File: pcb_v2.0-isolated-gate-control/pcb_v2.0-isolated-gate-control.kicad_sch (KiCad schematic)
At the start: 94 parts, among them J1 ServoLock, J10 Buttons, J11 2x encoder, J12 Screw_Terminal_01x06, J13 Relay VFD2 [NO, COM, NC], J14 GND-P, J15 Power-Servo-12V, J16 Power-LightBarrier-12V, J17 3V3 5V VDD, J18 GNDD, J2 supply, J3 12V-filtered, J4 light-barrier, reserve, J5 GND-P, J6 2x remoteControl, J7 Relay VFD1 [NO, COM, NC], J8 RS485, J9 limit, K1 RT314A24, K2 RT314A24, Q1 2N7000, Q2 2N7000, Q3 IRF5305, Q6 IRF5305, U1 esp32-devkit-v1_30Pin, U4 MAX485E, U5 L78S05CV_TO220, U6 ULN2803A

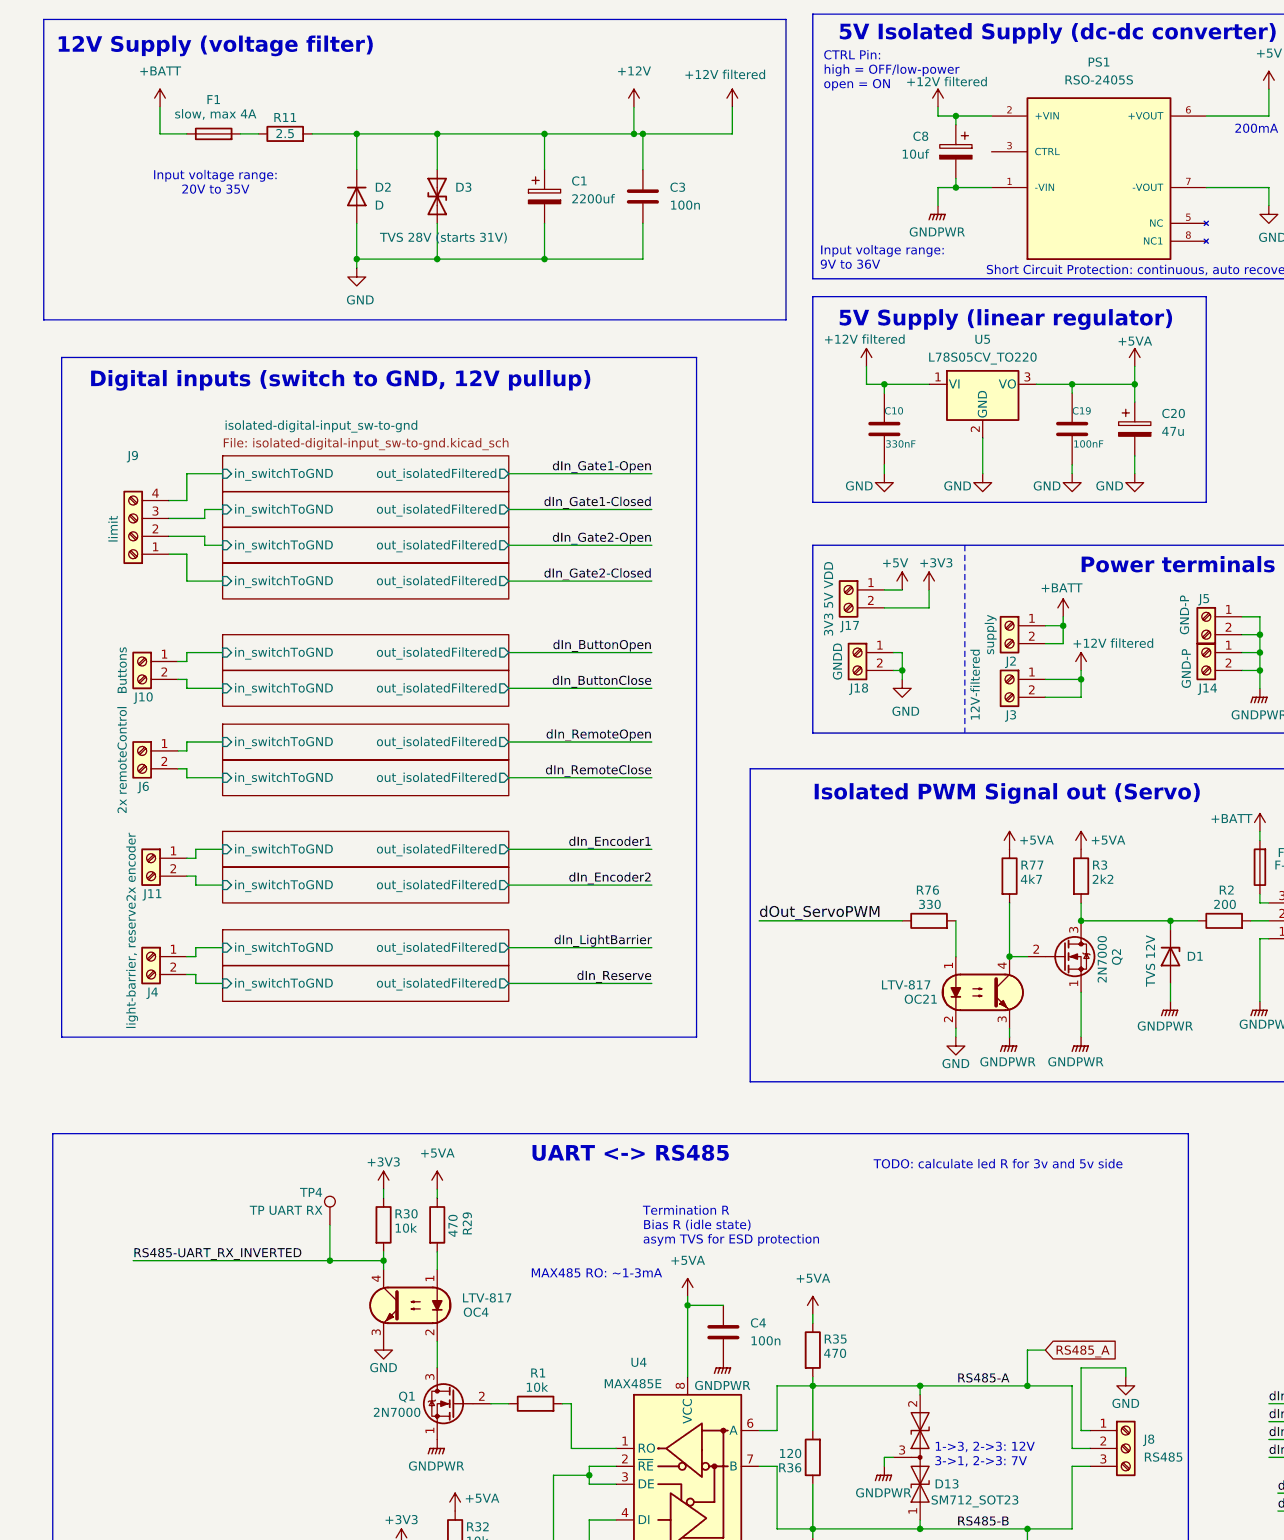
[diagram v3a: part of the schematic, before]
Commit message: pcb: change footprints + arrange groups individually for saving space
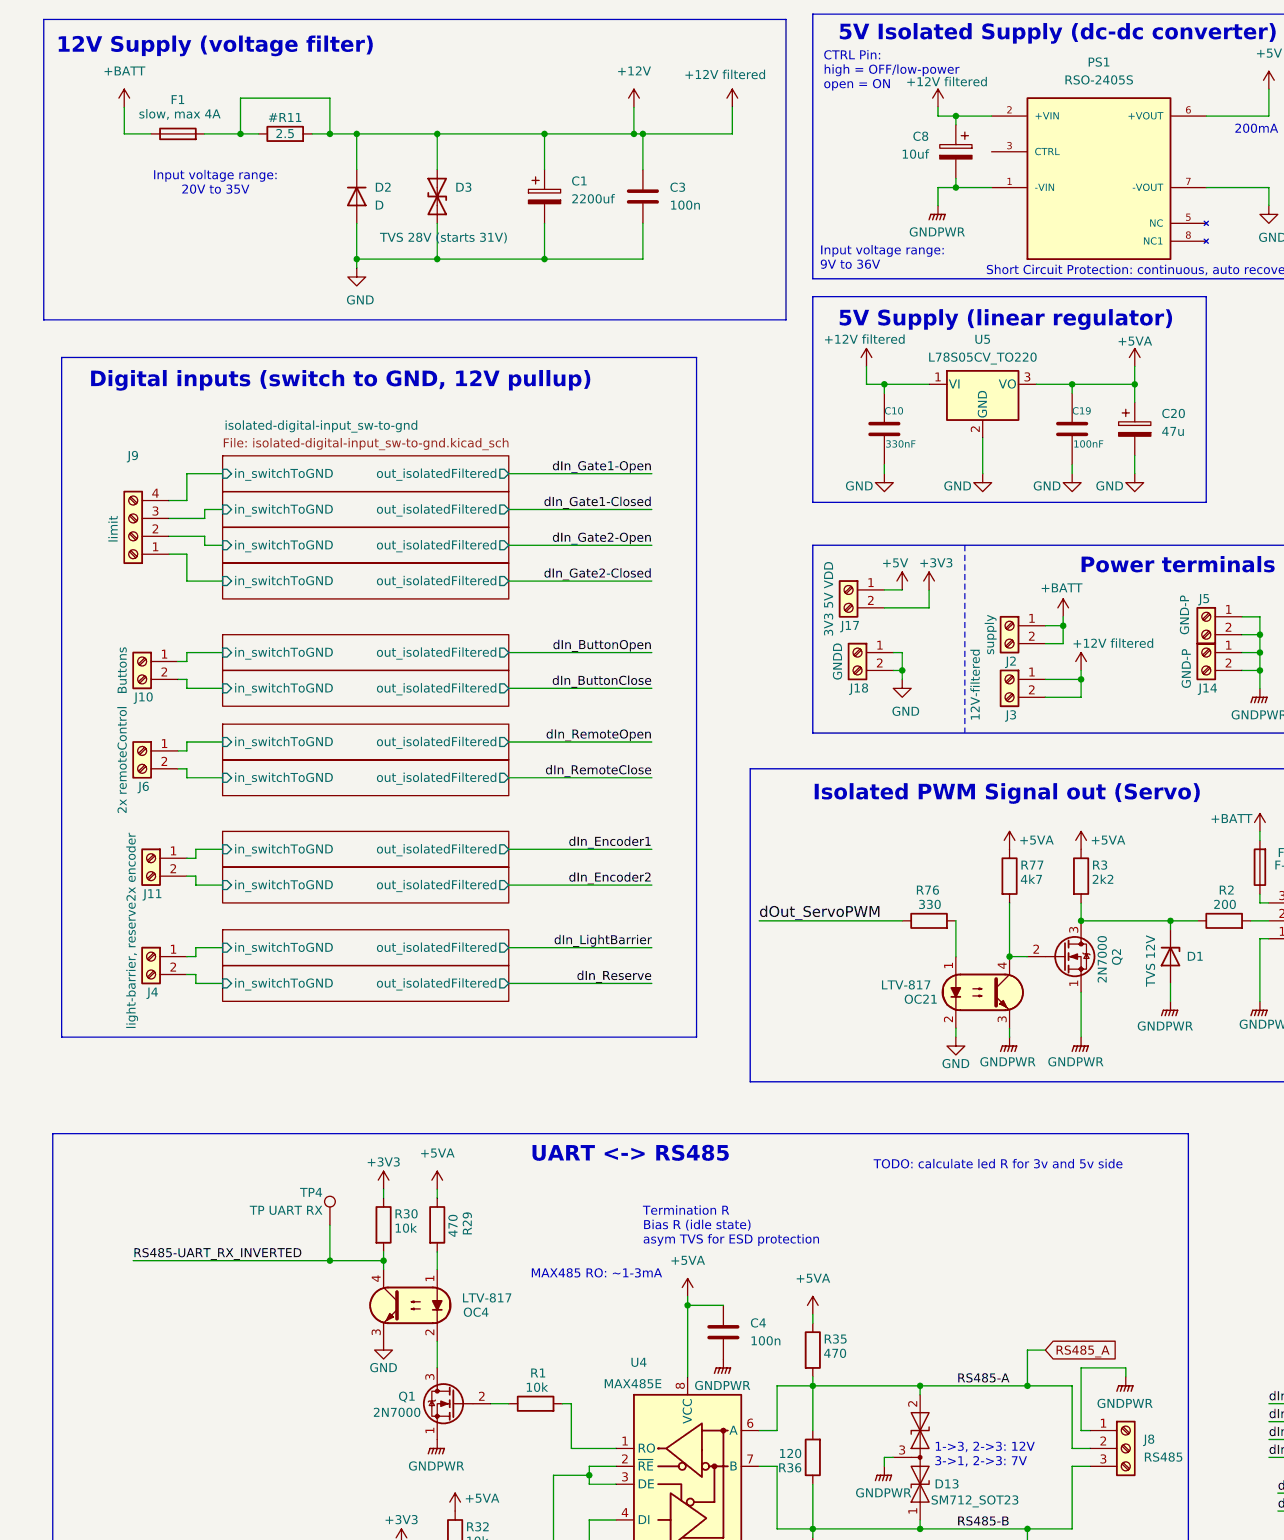
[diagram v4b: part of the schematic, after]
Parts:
- D26, D27: footprint Diode_THT_AKL_Double:D_DO-27_P20.32mm_Horizontal -> Diode_THT:D_DO-201_P5.08mm_Vertical_KathodeUp
- R1, R10, R30, R39, R40, R41, R65, R66, R67, R68, R71, R72, R76, R81, R82: footprint Resistor_THT:R_Axial_DIN0207_L6.3mm_D2.5mm_P10.16mm_Horizontal -> Resistor_THT:R_Axial_DIN0207_L6.3mm_D2.5mm_P2.54mm_Vertical
- renumbered R11 to #R11
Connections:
- net +12V: now also #R11.1, F1.2
- net GND: no longer J8.1 (Pin_1)
- net GNDPWR: now also J8.1 (Pin_1)
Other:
- moved on the sheet: F1
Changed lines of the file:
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@@
 	)
 	(junction
+		(at 46.99 34.29)
+		(diameter 0)
+		(color 0 0 0 0)
+	)
+	(junction
 		(at 191.77 105.41)
 		(diameter 0)
@@
 	)
 	(junction
+		(at 59.69 34.29)
+		(diameter 0)
+		(color 0 0 0 0)
+	)
+	(junction
 		(at 166.37 146.05)
 		(diameter 0)
@@
 	(wire
 		(pts
+			(xy 59.69 34.29) (xy 59.69 29.21)
+		)
+		(stroke
+			(width 0)
+			(type default)
+		)
+	)
+	(wire
+		(pts
 			(xy 138.43 71.12) (xy 138.43 69.85)
 		)
@@
 	(wire
 		(pts
+			(xy 46.99 34.29) (xy 49.53 34.29)
+		)
+		(stroke
+			(width 0)
+			(type default)
+		)
+	)
+	(wire
+		(pts
 			(xy 93.98 220.98) (xy 100.33 220.98)
 		)
@@
 	(wire
 		(pts
+			(xy 59.69 34.29) (xy 63.5 34.29)
+		)
+		(stroke
+			(width 0)
+			(type default)
+		)
+	)
+	(wire
+		(pts
 			(xy 281.94 237.49) (xy 311.15 237.49)
 		)
@@
 	(wire
 		(pts
-			(xy 57.15 34.29) (xy 63.5 34.29)
+			(xy 59.69 29.21) (xy 46.99 29.21)
+		)
+		(stroke
+			(width 0)
+			(type default)
+		)
+	)
+	(wire
+		(pts
+			(xy 57.15 34.29) (xy 59.69 34.29)
 		)
 		(stroke
@@
 	(wire
 		(pts
+			(xy 46.99 29.21) (xy 46.99 34.29)
+		)
+		(stroke
+			(width 0)
+			(type default)
+		)
+	)
+	(wire
+		(pts
 			(xy 166.37 143.51) (xy 166.37 146.05)
 		)
@@
 	(wire
 		(pts
-			(xy 46.99 34.29) (xy 49.53 34.29)
+			(xy 41.91 34.29) (xy 46.99 34.29)
 		)
 		(stroke
@@
 	(wire
 		(pts
-			(xy 35.56 34.29) (xy 39.37 34.29)
+			(xy 30.48 34.29) (xy 34.29 34.29)
 		)
 		(stroke
@@
 	(wire
 		(pts
-			(xy 35.56 30.48) (xy 35.56 34.29)
+			(xy 30.48 30.48) (xy 30.48 34.29)
 		)
 		(stroke
@@
 			)
 		)
-		(property "Footprint" "Resistor_THT:R_Axial_DIN0207_L6.3mm_D2.5mm_P10.16mm_Horizontal"
+		(property "Footprint" "Resistor_THT:R_Axial_DIN0207_L6.3mm_D2.5mm_P2.54mm_Vertical"
 			(at 88.9 216.408 90)
 			(effects
@@
 	)
 	(symbol
-		(lib_id "power:GND")
-		(at 172.72 210.82 0)
-		(unit 1)
-		(exclude_from_sim no)
-		(in_bom yes)
-		(on_board yes)
-		(dnp no)
-		(property "Reference" "#PWR059"
-			(at 172.72 217.17 0)
-			(effects
-				(font
-					(size 1.27 1.27)
-				)
-				(hide yes)
-			)
-		)
-		(property "Value" "GND"
-			(at 172.72 214.63 0)
-			(effects
-				(font
-					(size 1.27 1.27)
-				)
-			)
-		)
-		(property "Footprint" ""
-			(at 172.72 210.82 0)
-			(effects
-				(font
-					(size 1.27 1.27)
-				)
-				(hide yes)
-			)
-		)
-		(property "Datasheet" ""
-			(at 172.72 210.82 0)
-			(effects
-				(font
-					(size 1.27 1.27)
-				)
-				(hide yes)
-			)
-		)
-		(property "Description" "Power symbol creates a global label with name \"GND\" , ground"
-			(at 172.72 210.82 0)
-			(effects
-				(font
-					(size 1.27 1.27)
-				)
-				(hide yes)
-			)
-		)
-		(pin "1"
-		)
-		(instances
-			(project "vfd-interface-board"
-				(path "/ac76819f-1531-4fd0-a2aa-e864e761b2bd"
-					(reference "#PWR059")
-					(unit 1)
-				)
-			)
-		)
-	)
-	(symbol
 		(lib_id "power:GNDPWR")
 		(at 74.93 219.71 0)
@@
 			)
 		)
-		(property "Footprint" "Resistor_THT:R_Axial_DIN0207_L6.3mm_D2.5mm_P10.16mm_Horizontal"
+		(property "Footprint" "Resistor_THT:R_Axial_DIN0207_L6.3mm_D2.5mm_P2.54mm_Vertical"
 			(at 249.682 50.8 90)
 			(effects
@@
 	(symbol
 		(lib_id "Device:Fuse")
-		(at 43.18 34.29 90)
+		(at 38.1 34.29 90)
 		(unit 1)
 		(exclude_from_sim no)
@@
 		(dnp no)
 		(property "Reference" "F1"
-			(at 43.18 29.464 90)
+			(at 38.1 29.464 90)
 			(effects
 				(font
@@
 		)
 		(property "Value" "slow, max 4A"
-			(at 43.434 31.496 90)
+			(at 38.354 31.496 90)
 			(effects
 				(font
@@
 		)
 		(property "Footprint" "misc_libJonny:Fuseholder_Automotive-Regular_Fuse19x5x18mm_Footprint21x8mm_Inline"
-			(at 43.18 36.068 90)
+			(at 38.1 36.068 90)
 			(effects
 				(font
@@
 		)
 		(property "Datasheet" "~"
-			(at 43.18 34.29 0)
+			(at 38.1 34.29 0)
 			(effects
 				(font
@@
 		)
 		(property "Description" "Fuse"
-			(at 43.18 34.29 0)
+			(at 38.1 34.29 0)
 			(effects
 				(font
@@
 			)
 		)
-		(property "Footprint" "Resistor_THT:R_Axial_DIN0207_L6.3mm_D2.5mm_P10.16mm_Horizontal"
+		(property "Footprint" "Resistor_THT:R_Axial_DIN0207_L6.3mm_D2.5mm_P2.54mm_Vertical"
 			(at 249.682 147.32 90)
 			(effects
@@
 		(on_board yes)
 		(dnp no)
-		(property "Reference" "R11"
+		(property "Reference" "#R11"
 			(at 53.34 32.004 90)
 			(effects
@@
 			(project "vfd-interface-board"
 				(path "/ac76819f-1531-4fd0-a2aa-e864e761b2bd"
-					(reference "R11")
+					(reference "#R11")
 					(unit 1)
 				)
@@
 	)
 	(symbol
+		(lib_id "power:GNDPWR")
+		(at 172.72 210.82 0)
+		(unit 1)
+		(exclude_from_sim no)
+		(in_bom yes)
+		(on_board yes)
+		(dnp no)
+		(fields_autoplaced yes)
+		(property "Reference" "#PWR021"
+			(at 172.72 215.9 0)
+			(effects
+				(font
+					(size 1.27 1.27)
+				)
+				(hide yes)
+			)
+		)
+		(property "Value" "GNDPWR"
+			(at 172.593 214.63 0)
+			(effects
+				(font
+					(size 1.27 1.27)
+				)
+			)
+		)
+		(property "Footprint" ""
+			(at 172.72 212.09 0)
+			(effects
+				(font
+					(size 1.27 1.27)
+				)
+				(hide yes)
+			)
+		)
+		(property "Datasheet" ""
+			(at 172.72 212.09 0)
+			(effects
+				(font
+					(size 1.27 1.27)
+				)
+				(hide yes)
+			)
+		)
+		(property "Description" "Power symbol creates a global label with name \"GNDPWR\" , global ground"
+			(at 172.72 210.82 0)
+			(effects
+				(font
+					(size 1.27 1.27)
+				)
+				(hide yes)
+			)
+		)
+		(pin "1"
+		)
+		(instances
+			(project "pcb_v2.0-isolated-gate-control"
+				(path "/ac76819f-1531-4fd0-a2aa-e864e761b2bd"
+					(reference "#PWR021")
+					(unit 1)
+				)
+			)
+		)
+	)
+	(symbol
 		(lib_id "power:+5V")
 		(at 193.04 27.94 0)
@@
 			)
 		)
-		(property "Footprint" "Resistor_THT:R_Axial_DIN0207_L6.3mm_D2.5mm_P10.16mm_Horizontal"
+		(property "Footprint" "Resistor_THT:R_Axial_DIN0207_L6.3mm_D2.5mm_P2.54mm_Vertical"
 			(at 237.49 43.688 90)
 			(effects
@@
 			)
 		)
-		(property "Footprint" "Resistor_THT:R_Axial_DIN0207_L6.3mm_D2.5mm_P10.16mm_Horizontal"
+		(property "Footprint" "Resistor_THT:R_Axial_DIN0207_L6.3mm_D2.5mm_P2.54mm_Vertical"
 			(at 249.682 99.06 90)
 			(effects
@@
 			)
 		)
-		(property "Footprint" "Resistor_THT:R_Axial_DIN0207_L6.3mm_D2.5mm_P10.16mm_Horizontal"
+		(property "Footprint" "Resistor_THT:R_Axial_DIN0207_L6.3mm_D2.5mm_P2.54mm_Vertical"
 			(at 249.682 123.19 90)
 			(effects
@@
 			)
 		)
-		(property "Footprint" "Resistor_THT:R_Axial_DIN0207_L6.3mm_D2.5mm_P10.16mm_Horizontal"
+		(property "Footprint" "Resistor_THT:R_Axial_DIN0207_L6.3mm_D2.5mm_P2.54mm_Vertical"
 			(at 237.49 140.208 90)
 			(effects
@@
 			)
 		)
-		(property "Footprint" "Diode_THT_AKL_Double:D_DO-27_P20.32mm_Horizontal"
+		(property "Footprint" "Diode_THT:D_DO-201_P5.08mm_Vertical_KathodeUp"
 			(at 381 134.62 0)
 			(effects
@@
 			)
 		)
-		(property "Footprint" "Diode_THT_AKL_Double:D_DO-27_P20.32mm_Horizontal"
+		(property "Footprint" "Diode_THT:D_DO-201_P5.08mm_Vertical_KathodeUp"
 			(at 381 107.95 0)
 			(effects
@@
 			)
 		)
-		(property "Footprint" "Resistor_THT:R_Axial_DIN0207_L6.3mm_D2.5mm_P10.16mm_Horizontal"
+		(property "Footprint" "Resistor_THT:R_Axial_DIN0207_L6.3mm_D2.5mm_P2.54mm_Vertical"
 			(at 237.49 164.338 90)
 			(effects
@@
 			)
 		)
-		(property "Footprint" "Resistor_THT:R_Axial_DIN0207_L6.3mm_D2.5mm_P10.16mm_Horizontal"
+		(property "Footprint" "Resistor_THT:R_Axial_DIN0207_L6.3mm_D2.5mm_P2.54mm_Vertical"
 			(at 249.682 26.67 90)
 			(effects
@@
 			)
 		)
-		(property "Footprint" "Resistor_THT:R_Axial_DIN0207_L6.3mm_D2.5mm_P10.16mm_Horizontal"
+		(property "Footprint" "Resistor_THT:R_Axial_DIN0207_L6.3mm_D2.5mm_P2.54mm_Vertical"
 			(at 65.532 189.23 90)
 			(effects
@@
 			)
 		)
-		(property "Footprint" "Resistor_THT:R_Axial_DIN0207_L6.3mm_D2.5mm_P10.16mm_Horizontal"
+		(property "Footprint" "Resistor_THT:R_Axial_DIN0207_L6.3mm_D2.5mm_P2.54mm_Vertical"
 			(at 249.682 74.93 90)
 			(effects
@@
 			)
 		)
-		(property "Footprint" "Resistor_THT:R_Axial_DIN0207_L6.3mm_D2.5mm_P10.16mm_Horizontal"
+		(property "Footprint" "Resistor_THT:R_Axial_DIN0207_L6.3mm_D2.5mm_P2.54mm_Vertical"
 			(at 237.49 91.948 90)
 			(effects
@@
 			)
 		)
-		(property "Footprint" "Resistor_THT:R_Axial_DIN0207_L6.3mm_D2.5mm_P10.16mm_Horizontal"
+		(property "Footprint" "Resistor_THT:R_Axial_DIN0207_L6.3mm_D2.5mm_P2.54mm_Vertical"
 			(at 237.49 67.818 90)
 			(effects
@@
 	(symbol
 		(lib_id "power:+BATT")
-		(at 35.56 30.48 0)
+		(at 30.48 30.48 0)
 		(unit 1)
 		(exclude_from_sim no)
@@
 		(fields_autoplaced yes)
 		(property "Reference" "#PWR02"
-			(at 35.56 34.29 0)
+			(at 30.48 34.29 0)
 			(effects
 				(font
@@
 		)
 		(property "Value" "+BATT"
-			(at 35.56 25.4 0)
+			(at 30.48 25.4 0)
 			(effects
 				(font
@@
 		)
 		(property "Footprint" ""
-			(at 35.56 30.48 0)
+			(at 30.48 30.48 0)
 			(effects
 				(font
@@
 		)
 		(property "Datasheet" ""
-			(at 35.56 30.48 0)
+			(at 30.48 30.48 0)
 			(effects
 				(font
@@
 		)
 		(property "Description" "Power symbol creates a global label with name \"+BATT\""
-			(at 35.56 30.48 0)
+			(at 30.48 30.48 0)
 			(effects
 				(font
@@
 			)
 		)
-		(property "Footprint" "Resistor_THT:R_Axial_DIN0207_L6.3mm_D2.5mm_P10.16mm_Horizontal"
+		(property "Footprint" "Resistor_THT:R_Axial_DIN0207_L6.3mm_D2.5mm_P2.54mm_Vertical"
 			(at 144.78 147.828 90)
 			(effects
@@
 			)
 		)
-		(property "Footprint" "Resistor_THT:R_Axial_DIN0207_L6.3mm_D2.5mm_P10.16mm_Horizontal"
+		(property "Footprint" "Resistor_THT:R_Axial_DIN0207_L6.3mm_D2.5mm_P2.54mm_Vertical"
 			(at 237.49 116.078 90)
 			(effects
